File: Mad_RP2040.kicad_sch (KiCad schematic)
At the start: 26 parts, among them J1 USB_C_Receptacle, SW1 SW_SPST, SW2 SW_SPST, U0 PCB, U1 ECMF02-2AMX6

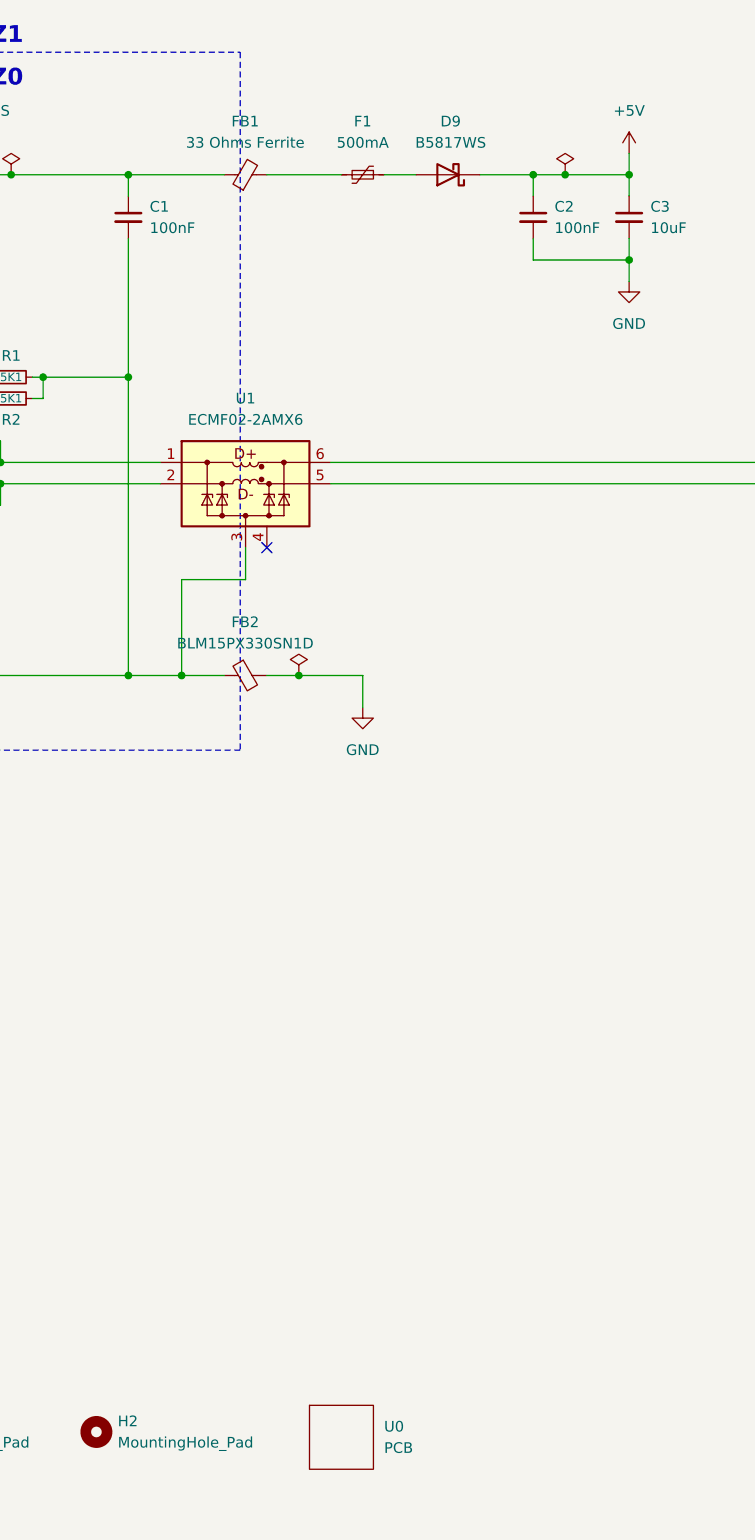
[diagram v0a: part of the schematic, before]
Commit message: 1 Add Panel (#2)
* #1 Add panel file and updated github action

* #1 Test for if panel file exhists

* #1 Rejig github actions

* Update job descriptions

* Add board tabs

* adjust panel array

* Add verbose

* Try using container method for building datapack

* Test custom action

* Update workflow

* Minor track work update and

* Add USB diff trace calcs and reroute usb traces

* Enable verbose

* Comment out second build

* Update value to mpn

* Update value to mpn

* #2 Update panel tabs
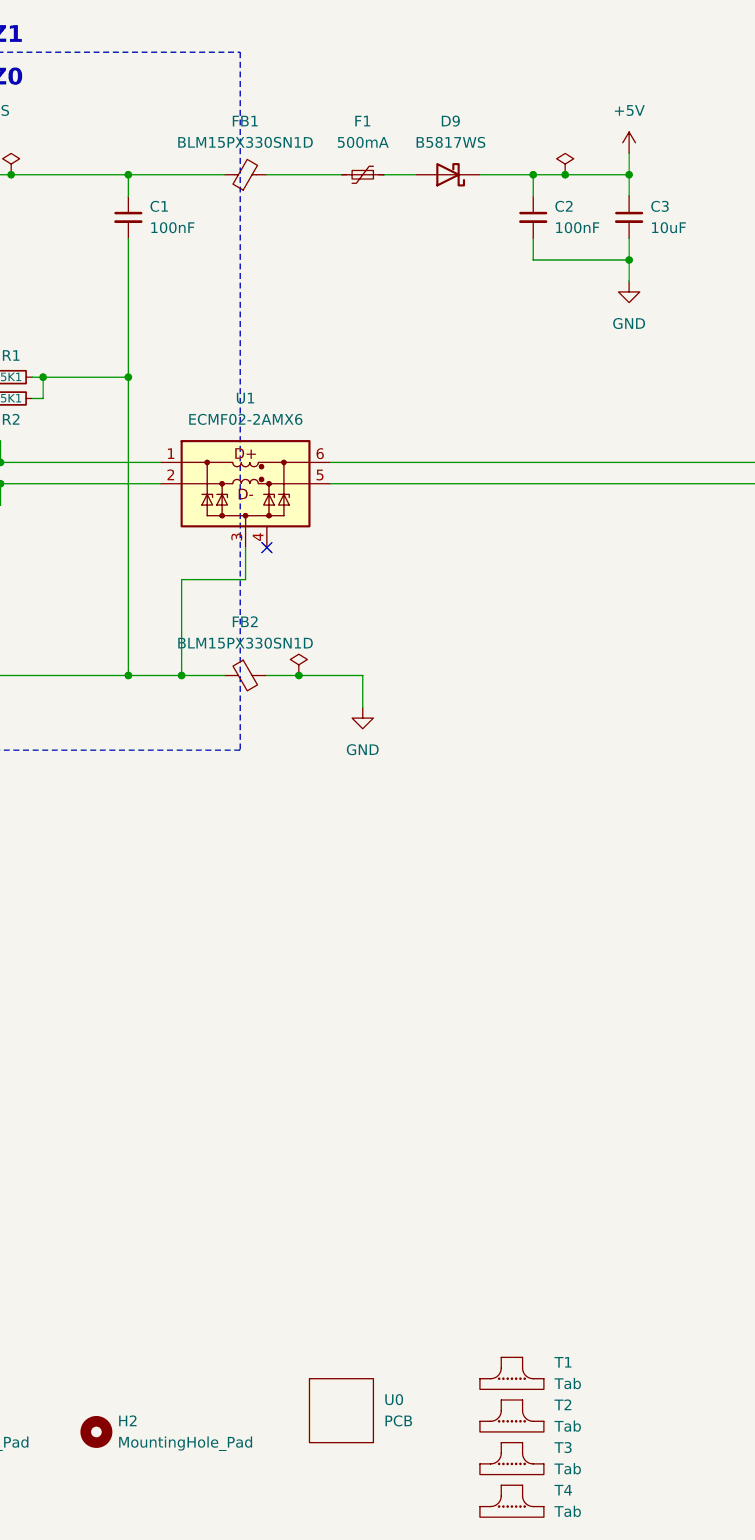
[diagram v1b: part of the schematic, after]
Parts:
- added T1, T2, T3, T4: Tab, PCM_kikit:Tab, symbol PCM_kikit:Tab
- FB1: value 33 Ohms Ferrite -> BLM15PX330SN1D
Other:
- moved on the sheet: U0

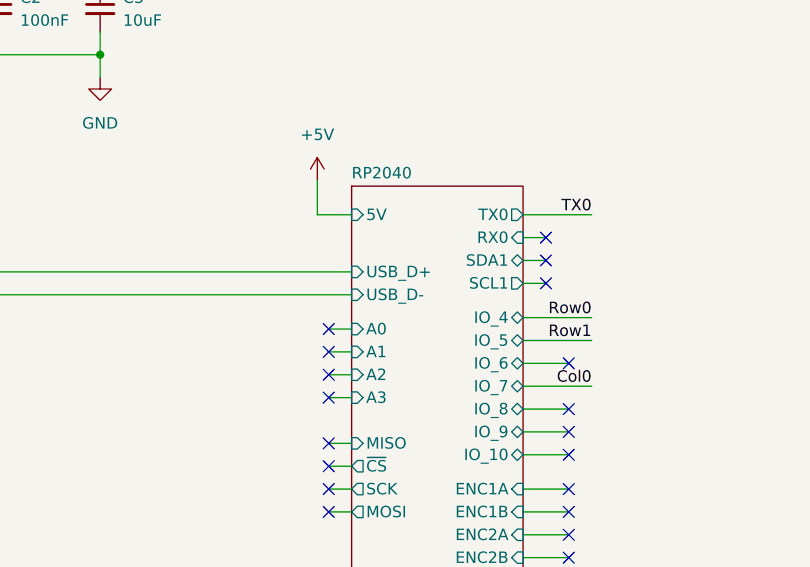
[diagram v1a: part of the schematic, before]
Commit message: Update usb data pins, update to fix 3v3 reg not adj
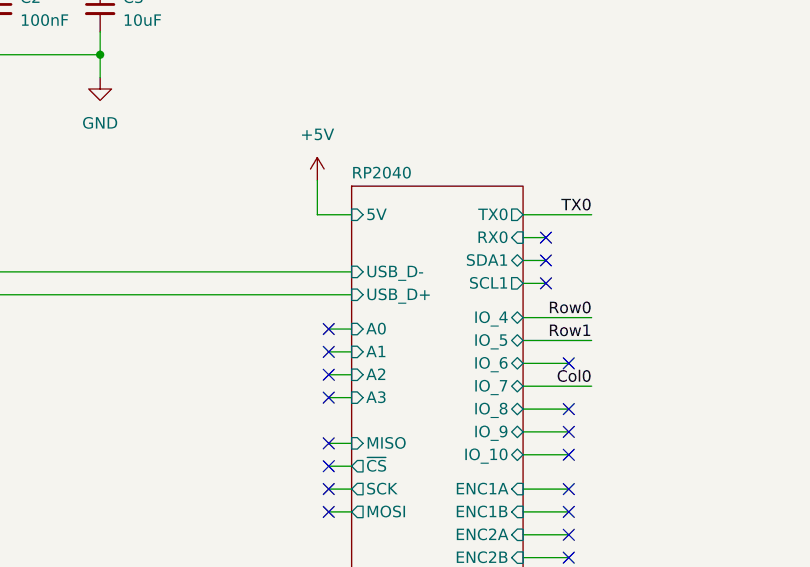
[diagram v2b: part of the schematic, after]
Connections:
- net RP2040/USB_D+: now also U1.5 (D-_out); no longer U1.6 (D+_out)
- net RP2040/USB_D-: now also U1.6 (D+_out); no longer U1.5 (D-_out)
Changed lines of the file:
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@@
 		)
 		(pin "USB_D+" input
-			(at 153.67 68.58 180)
+			(at 153.67 71.12 180)
 			(effects
 				(font
@@
 		)
 		(pin "USB_D-" input
-			(at 153.67 71.12 180)
+			(at 153.67 68.58 180)
 			(effects
 				(font

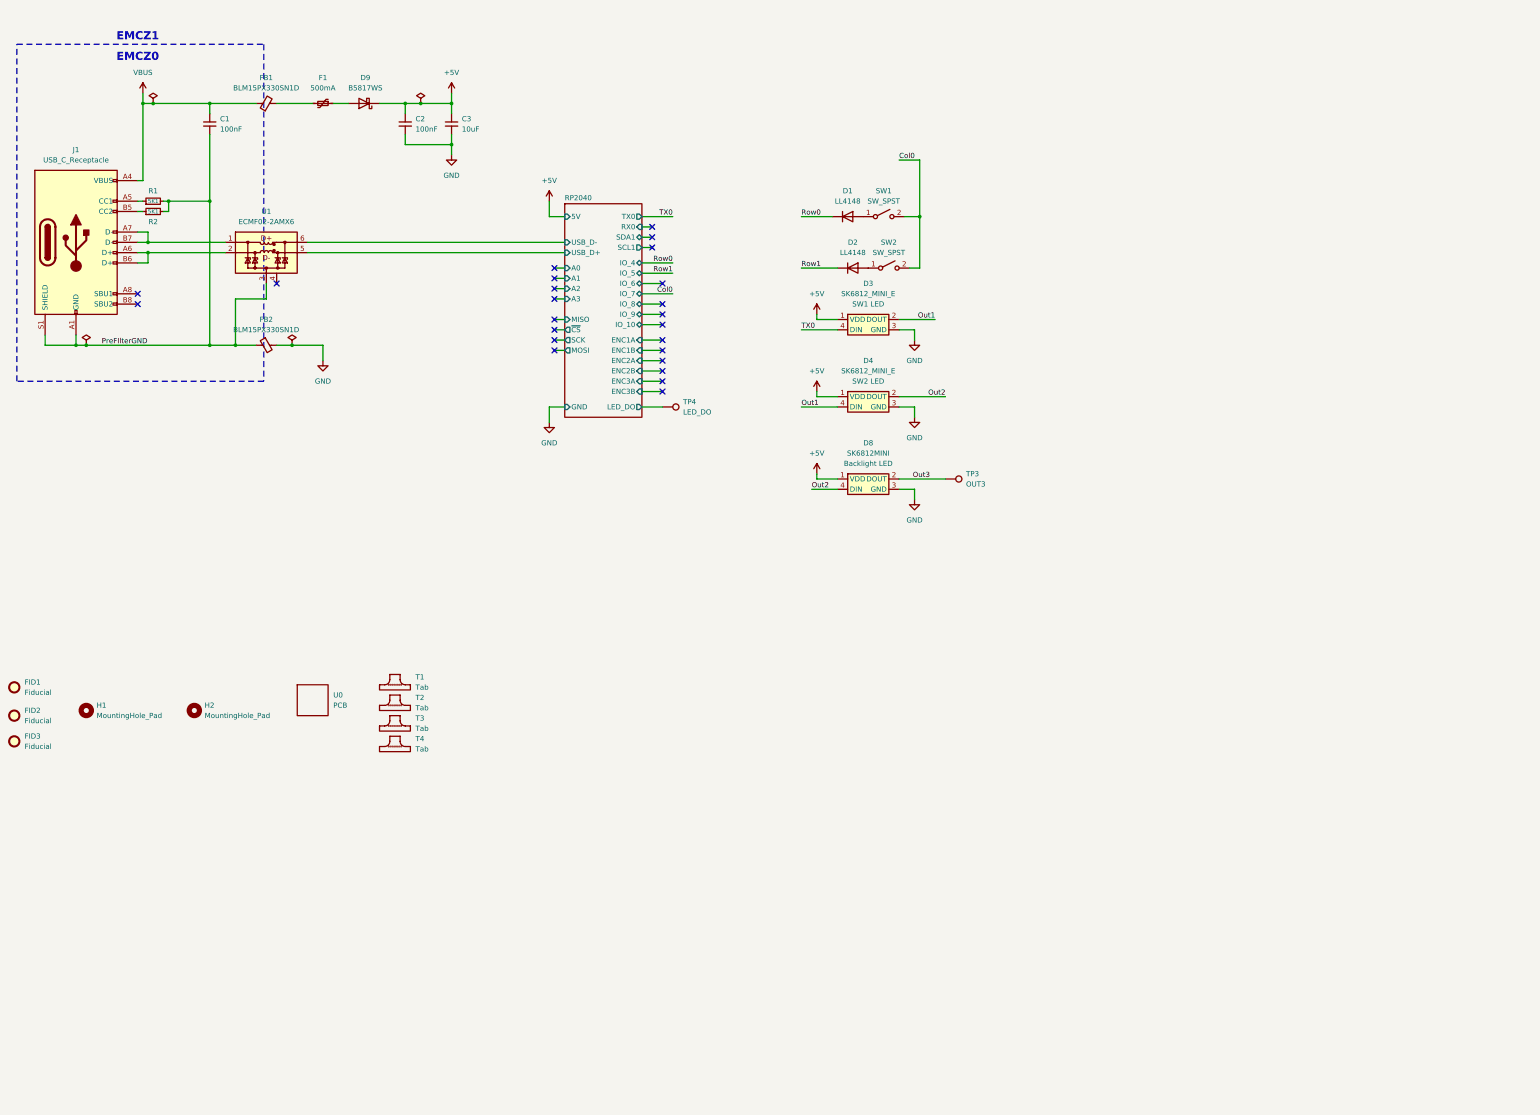
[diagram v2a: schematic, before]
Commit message: Update footprint on back light SK6812MINI LED, add more back lights.
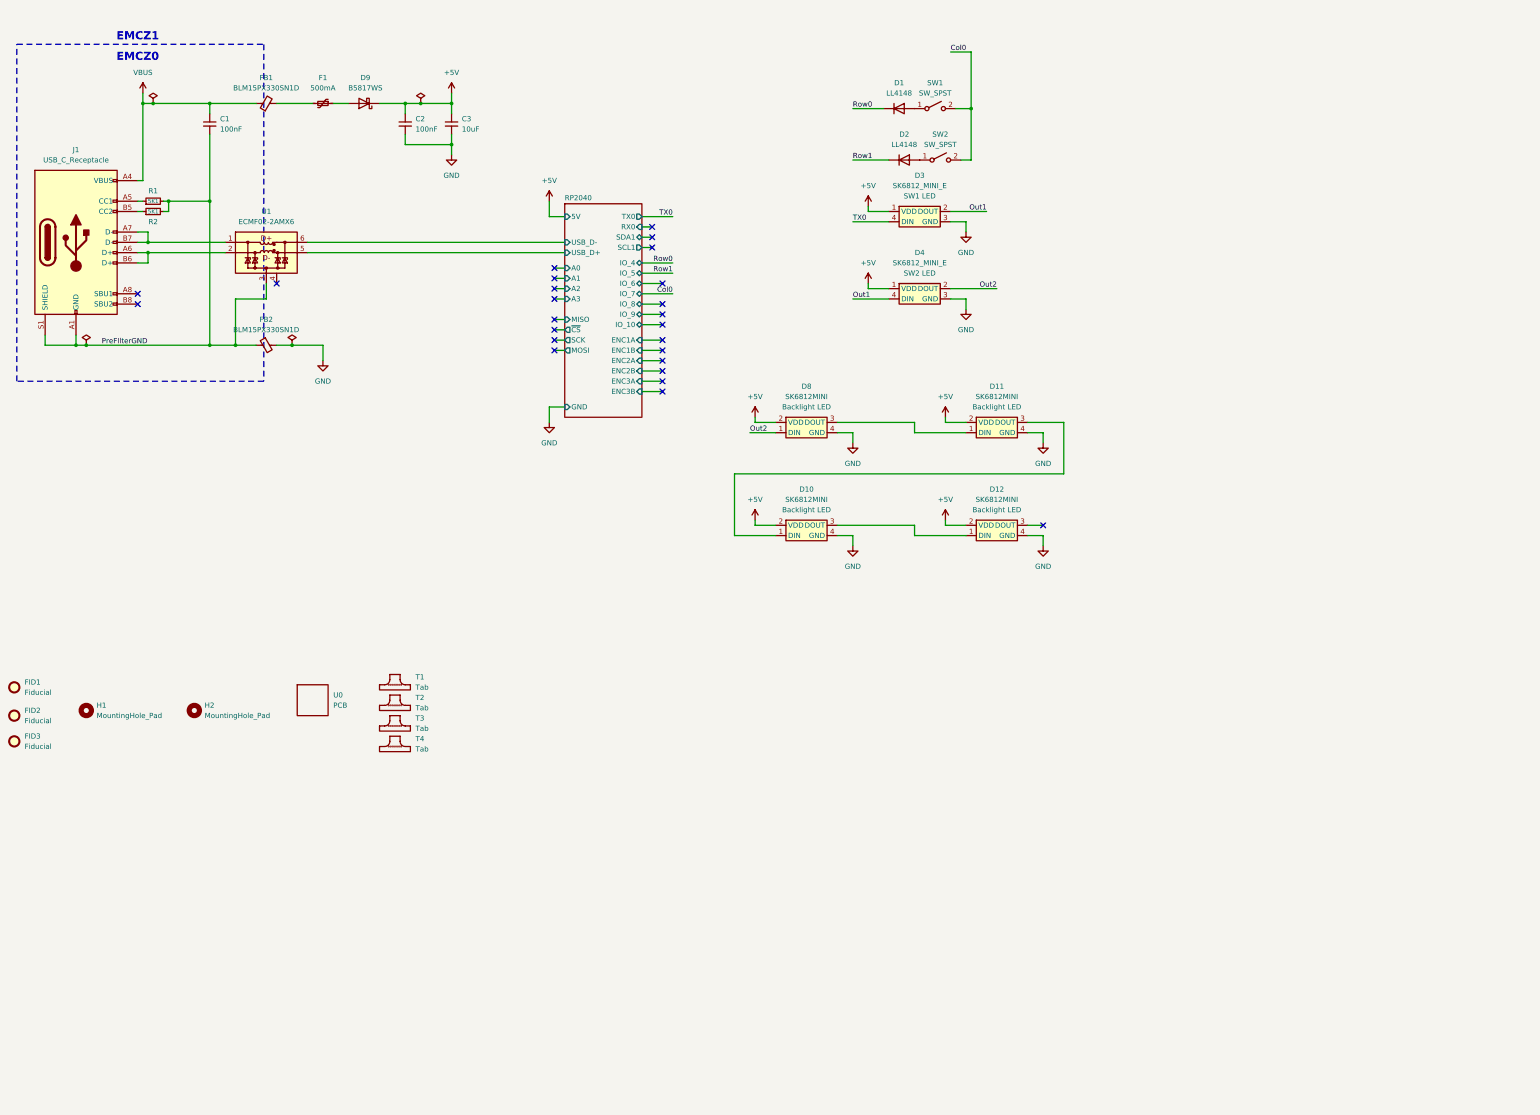
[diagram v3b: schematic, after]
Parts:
- removed TP3: OUT3, TestPoint:TestPoint_Pad_D1.0mm, symbol Connector:TestPoint
- removed TP4: LED_DO, TestPoint:TestPoint_Pad_D1.0mm, symbol Connector:TestPoint
- added D10, D11, D12: SK6812MINI, Mad_Footprints:SK6812MINI-012, symbol Mad_Symbols:SK6812MINI-012
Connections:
- net Out3 is gone; now on net +5V: D8.2 (VDD)
- net +5V: now also D10.2 (VDD), D11.2 (VDD), D12.2 (VDD); no longer D8.1 (VDD)
- net GND: now also D8.4 (GND), D10.4 (GND), D11.4 (GND), D12.4 (GND); no longer D8.3 (GND)
- net Out2: now also D8.1 (DIN); no longer D8.4 (DIN)
- new net: D11.1 (DIN), D8.3 (DOUT)
- new net: D10.1 (DIN), D11.3 (DOUT)
- new net: D10.3 (DOUT), D12.1 (DIN)
- no-connect marks 24 -> 25
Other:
- sheet RP2040 ports: added none; removed LED_DO
- moved on the sheet: D1, D2, D3, D4, D8, SW1, SW2

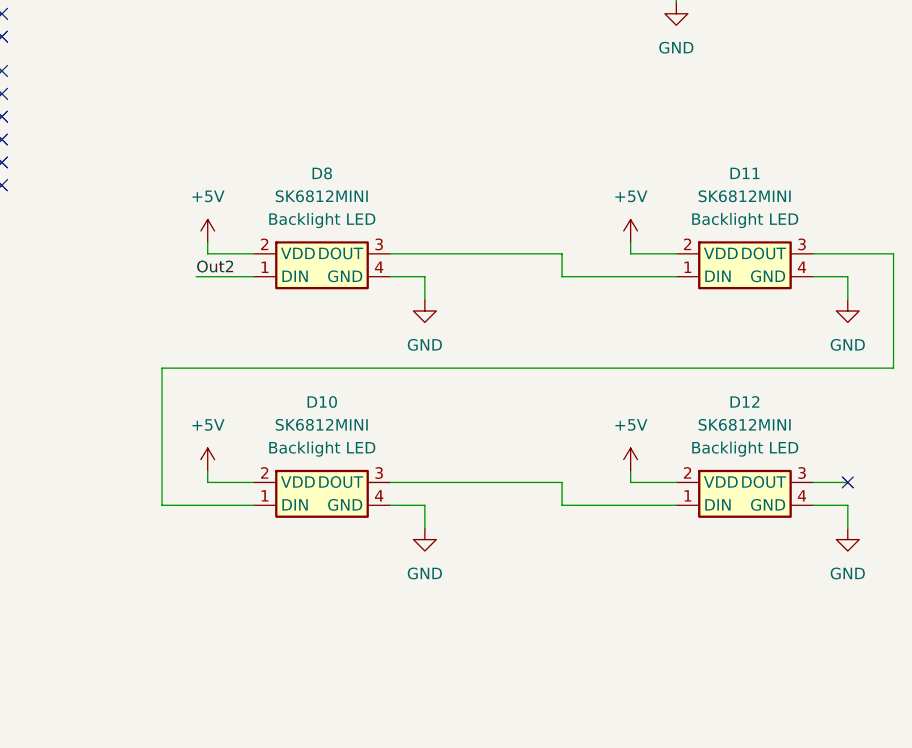
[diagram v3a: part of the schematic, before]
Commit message: Update PCB back light
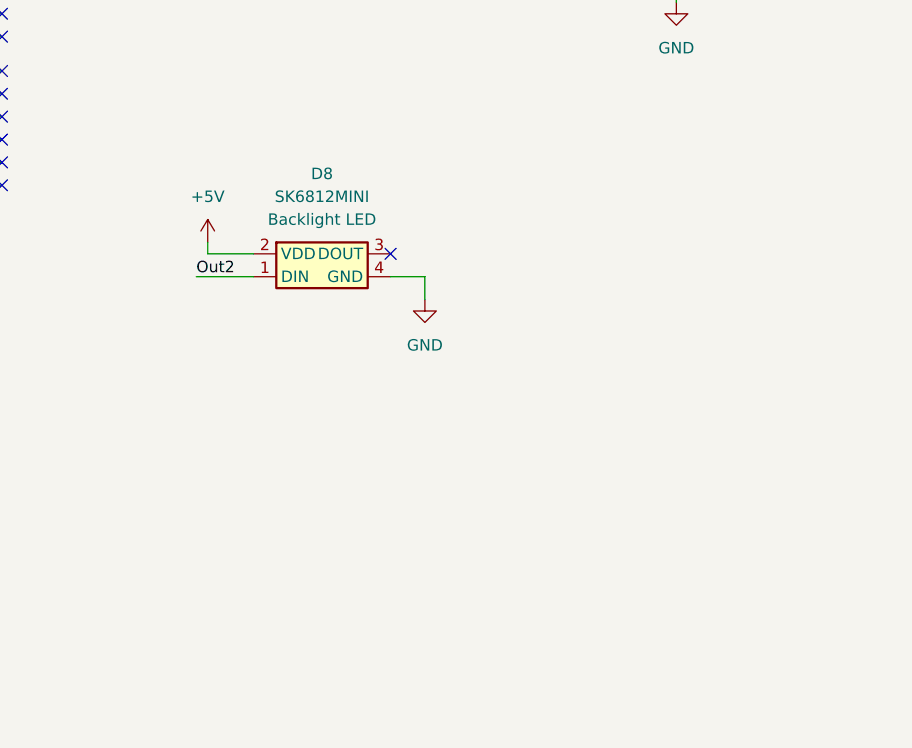
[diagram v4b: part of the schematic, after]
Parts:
- removed D10, D11, D12: SK6812MINI, Mad_Footprints:SK6812MINI-012, symbol Mad_Symbols:SK6812MINI-012
